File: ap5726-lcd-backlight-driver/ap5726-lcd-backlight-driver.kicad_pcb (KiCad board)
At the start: 2 copper layers, 22.9 x 14.8 mm, 9 parts, among them J1 Conn_01x05_Pin

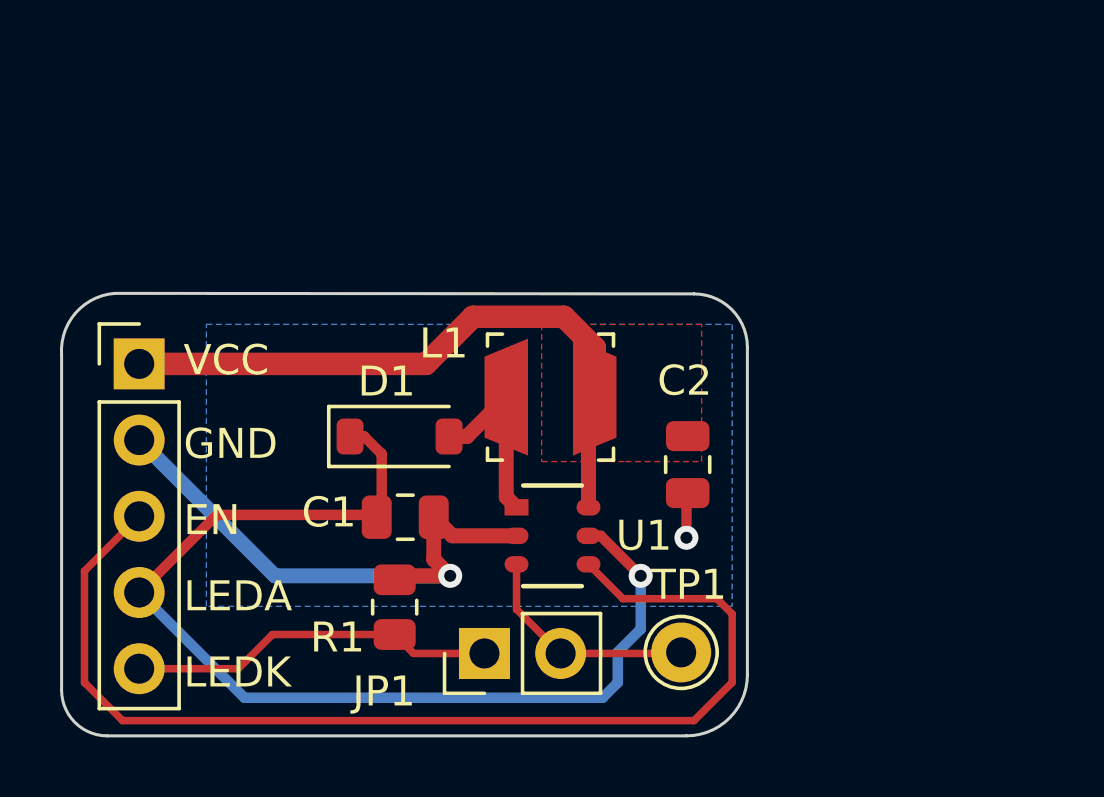
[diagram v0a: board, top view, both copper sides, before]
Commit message: Redo AP5726 pcb layout using fill zones.
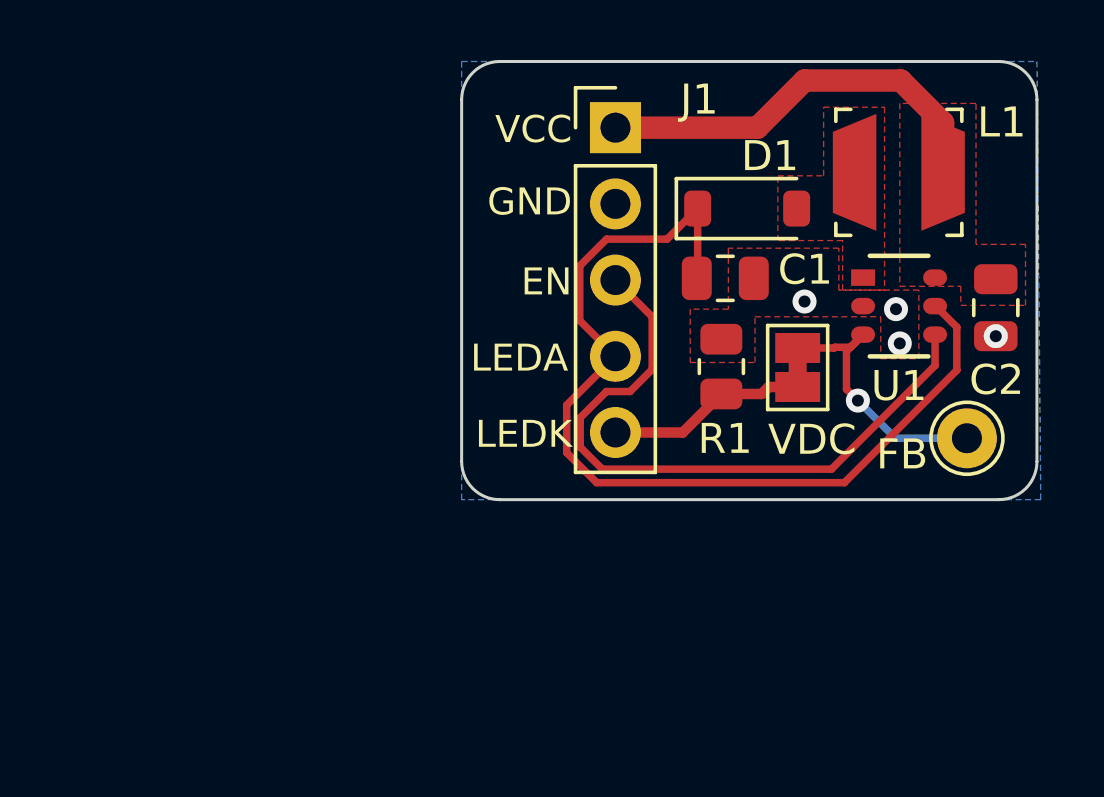
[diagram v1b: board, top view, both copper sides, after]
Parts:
- removed JP1: Jumper_2_Bridged, Connector_PinHeader_2.54mm:PinHeader_1x02_P2.54mm_Vertical
- removed TP1: TestPoint, TestPoint:TestPoint_THTPad_D2.0mm_Drill1.0mm
- added FB: TestPoint, TestPoint:TestPoint_THTPad_D2.0mm_Drill1.0mm, F.Cu at (165.1, 97.5)
- added VDC: Jumper_2_Bridged, Jumper:SolderJumper-2_P1.3mm_Bridged_Pad1.0x1.5mm, F.Cu at (159.4, 95.2)
- moved J1 17.7 mm to (153.3, 87.2)
- moved U1 13.9 mm to (162.8, 93.1)
- moved D1 13.9 mm to (157.7, 89.9)
- moved L1 13.8 mm to (162.8, 88.7)
- moved R1 13.5 mm to (156.9, 95.1)
- moved C1 13.3 mm to (157.0, 92.2)
- moved C2 11.5 mm to (166.0, 93.2)
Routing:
- net GND: track 20.9 -> 0.00 mm, vias 2 -> 4
- net /ENABLE: track 36.7 -> 22.1 mm
- net VCC: track 21.7 -> 13.8 mm
- net Net-(D1-A): track 6.26 -> 0.00 mm
- net /LED_K: track 12.2 -> 6.70 mm
- net /LED_A: track 36.3 -> 31.9 mm, vias 1 -> 0
- net Net-(JP1-B): track 7.61 -> 9.11 mm, vias 0 -> 1
- added copper zone on F.Cu, net GND
- added copper zone on F.Cu, net Net-(D1-A)
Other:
- board size 22.9 x 14.8 mm -> 19.2 x 14.6 mm

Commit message: More AP5726 pcb layout changes.
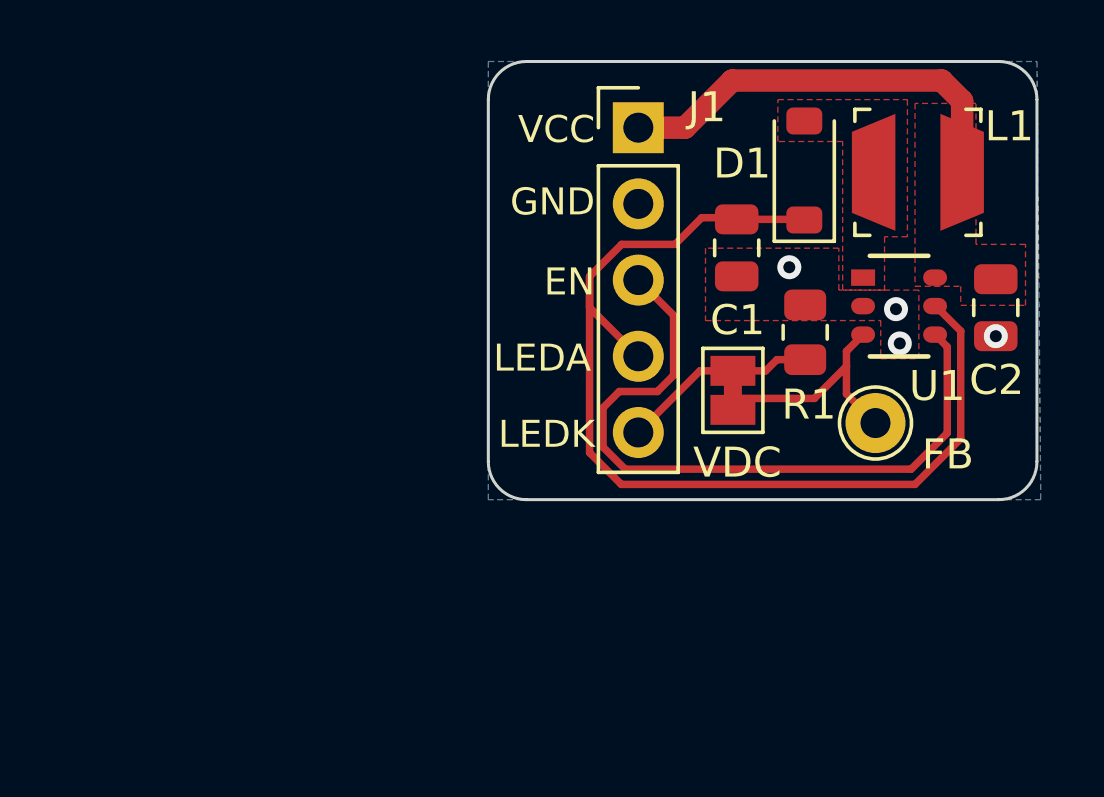
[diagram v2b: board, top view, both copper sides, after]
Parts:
- moved FB 3.09 mm to (162.0, 97.0)
- moved R1 3.02 mm to (159.7, 94.0)
- moved D1 2.29 mm to (159.6, 88.6), turned to 90 degrees
- moved VDC 2.29 mm to (157.3, 95.9), turned to -90 degrees
- moved C1 1.09 mm to (157.4, 91.2), turned to -90 degrees
- moved J1 0.76 mm to (154.1, 87.2)
- moved L1 0.63 mm to (163.4, 88.7)
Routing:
- net /LED_A: track 31.9 -> 35.4 mm
- net /ENABLE: track 22.1 -> 23.5 mm
- net Net-(JP1-B): track 9.11 -> 7.81 mm, vias 1 -> 0
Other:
- board size 19.2 x 14.6 mm -> 18.3 x 14.6 mm

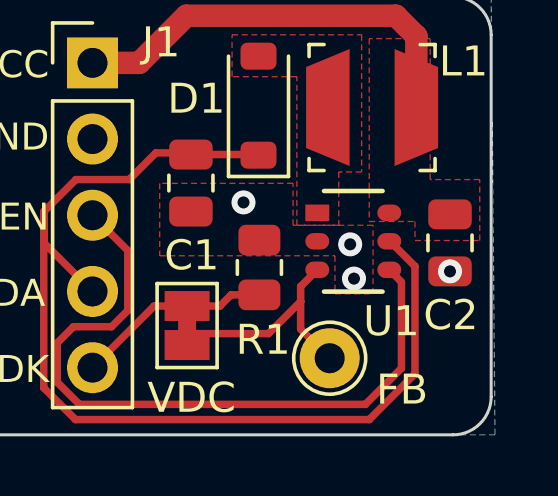
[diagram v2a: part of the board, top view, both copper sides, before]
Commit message: Move via off pad of C2 in AP5726 design.
Apparently, it's not good to put vias directly on pads (metal dome
switch trace design being an exception) because it may wick away solder
and also cause the surface to be uneven. An exception to this is when
you have a large thermal pad underneath an IC, in which case you may
want many vias spread out to provide surface area for solder to contact
as well as provide better heat distribution to the copper area on the
other side.
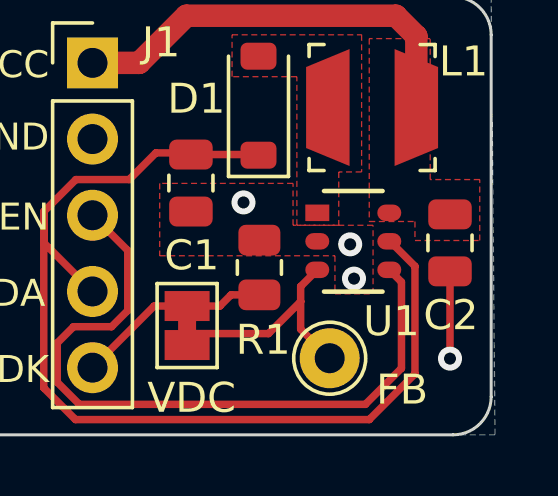
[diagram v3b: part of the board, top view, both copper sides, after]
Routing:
- net GND: track 0.00 -> 2.91 mm
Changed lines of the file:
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@@
   (segment (start 159.61 90.225) (end 159.631 90.246) (width 0.25) (layer "F.Cu") (net 1))
   (segment (start 164.846 97.536) (end 164.846 93.949471) (width 0.25) (layer "F.Cu") (net 1))
+  (segment (start 166.014 94.119) (end 166.014 97.028) (width 0.25) (layer "F.Cu") (net 2))
   (via (at 162.687 93.218) (size 0.8) (drill 0.4) (layers "F.Cu" "B.Cu") (free) (net 2))
   (via (at 162.814 94.361) (size 0.8) (drill 0.4) (layers "F.Cu" "B.Cu") (free) (net 2))
-  (via (at 166.014 94.119) (size 0.8) (drill 0.4) (layers "F.Cu" "B.Cu") (net 2))
+  (via (at 166.014 97.028) (size 0.8) (drill 0.4) (layers "F.Cu" "B.Cu") (net 2))
   (via (at 159.131 91.821) (size 0.8) (drill 0.4) (layers "F.Cu" "B.Cu") (free) (net 2))
   (segment (start 154.098 87.169) (end 155.655 87.169) (width 0.75) (layer "F.Cu") (net 3))
